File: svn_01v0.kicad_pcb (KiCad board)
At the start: 2 copper layers, 26 parts, among them J1 Screw_Terminal_01x05, Q1 IRF640, Q2 IRF640, U1 AD8542ARZ, U2 IR2110S, Y1 85kHz

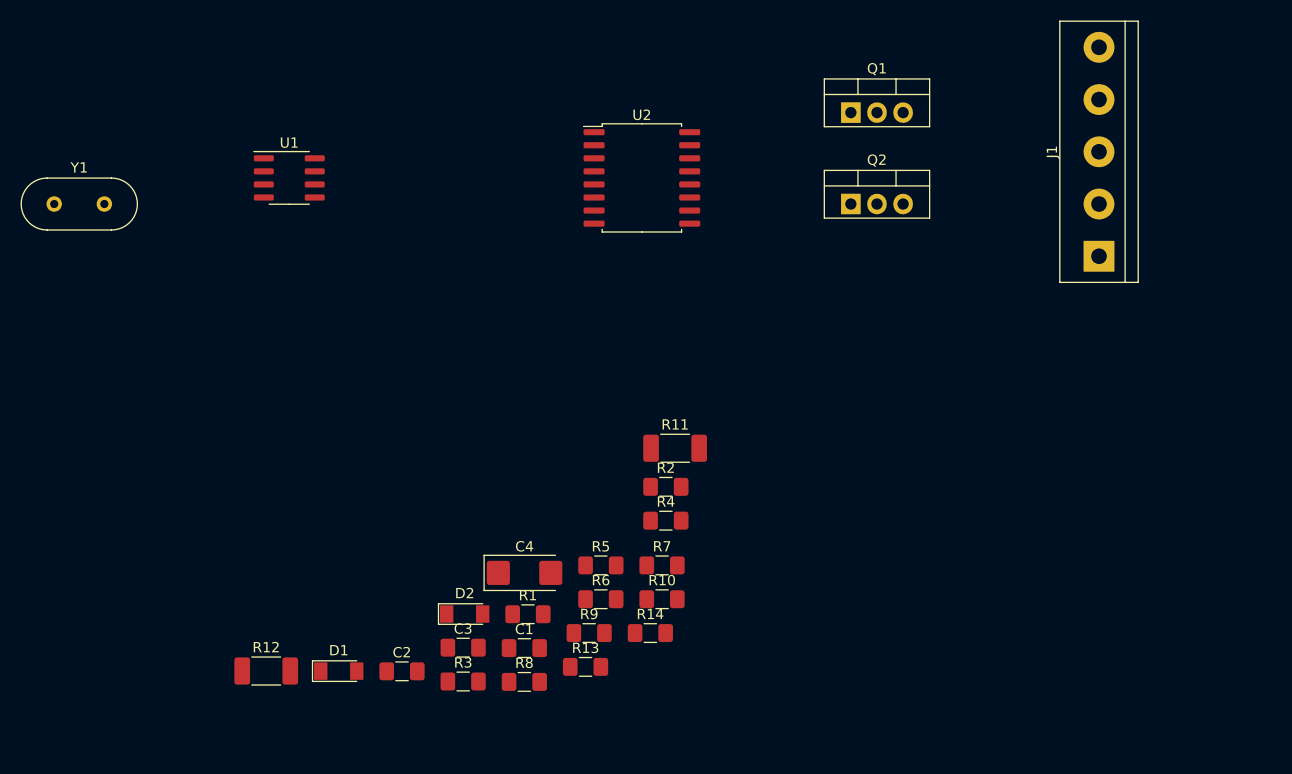
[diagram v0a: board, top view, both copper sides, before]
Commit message: Исправлена схема.
Исправлено подключенеи ОУ.
Разъем изменен на шести контактный.
Добавлен преобразователь 12В в 5В.
Добавлено несколько резисторов в обвязку ОУ.

Signed-off-by: bear.home <mihail_sheblykin@mail.ru>
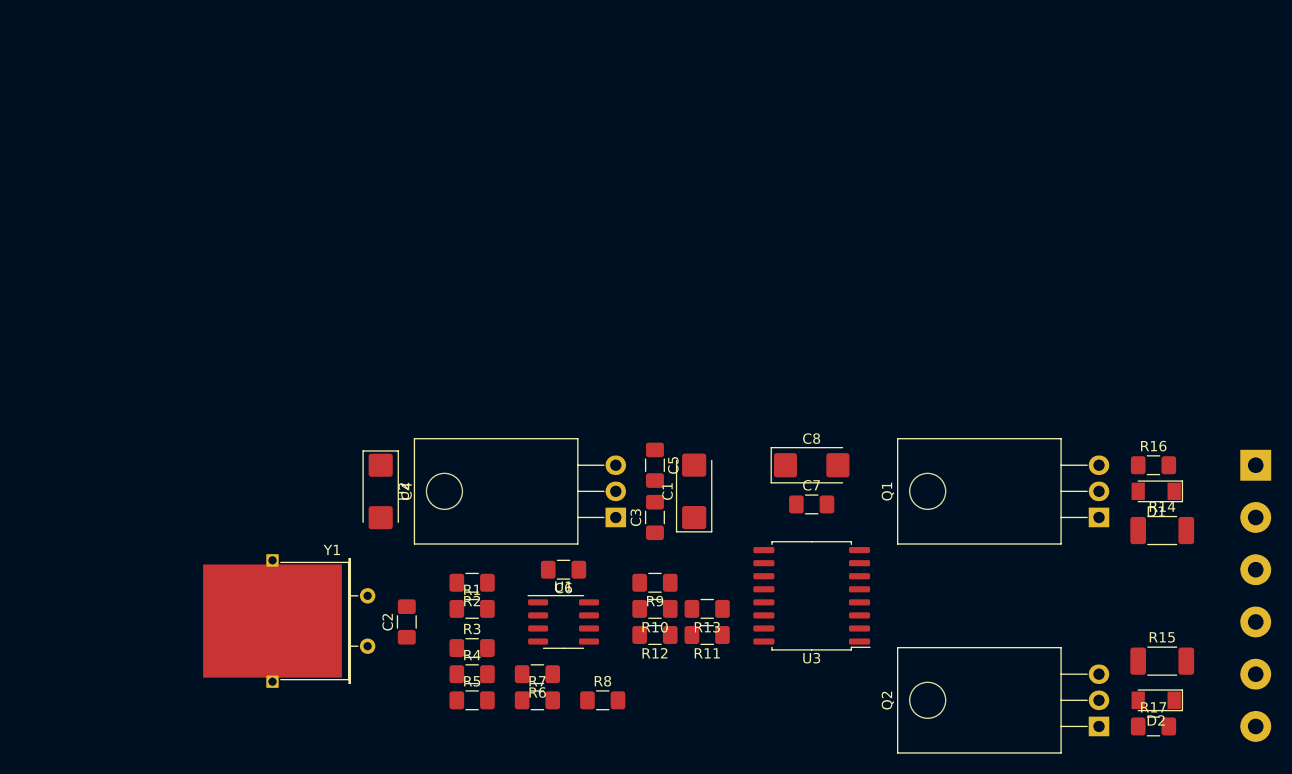
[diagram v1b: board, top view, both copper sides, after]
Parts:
- removed the R14 at (150.7, 90.0)
- added C1: 47uF x 16V, Capacitor_Tantalum_SMD:CP_EIA-6032-28_Kemet-C_Pad2.25x2.35mm_HandSolder, F.Cu at (154.9, 76.2)
- added C3: 100nF, Capacitor_SMD:C_1206_3216Metric_Pad1.42x1.75mm_HandSolder, F.Cu at (151.1, 78.7)
- added C4: 47uF x 16V, Capacitor_Tantalum_SMD:CP_EIA-6032-28_Kemet-C_Pad2.25x2.35mm_HandSolder, F.Cu at (124.5, 76.2)
- added C5: 100nF, Capacitor_SMD:C_1206_3216Metric_Pad1.42x1.75mm_HandSolder, F.Cu at (151.1, 73.7)
- added R12: 10k, Resistor_SMD:R_1206_3216Metric_Pad1.42x1.75mm_HandSolder, F.Cu at (151.1, 90.2)
- added R13: 10k, Resistor_SMD:R_1206_3216Metric_Pad1.42x1.75mm_HandSolder, F.Cu at (156.2, 87.6)
- added R17: 1k, Resistor_SMD:R_1206_3216Metric_Pad1.42x1.75mm_HandSolder, F.Cu at (199.6, 99.1)
- added R8: 10k, Resistor_SMD:R_1206_3216Metric_Pad1.42x1.75mm_HandSolder, F.Cu at (146.1, 96.5)
- added U2: LM7805_TO220, Package_TO_SOT_THT:TO-220-3_Horizontal_TabDown, F.Cu at (147.3, 78.7)
- C8: renamed from C4; value 22uF x 16V -> 47uF x 16V
- J1: value Screw_Terminal_01x05 -> Screw_Terminal_01x06; footprint TerminalBlock:TerminalBlock_bornier-5_P5.08mm -> TerminalBlock:TerminalBlock_bornier-6_P5.08mm; moved to B.Cu
- Q1, Q2: footprint Package_TO_SOT_THT:TO-220-3_Vertical -> Package_TO_SOT_THT:TO-220-3_Horizontal_TabDown
- R6: value 1k -> ?
- Y1: footprint Crystal:Crystal_HC49-U_Vertical -> Crystal:Crystal_HC49-U_Horizontal_1EP_style2
- moved R15 87.1 mm to (200.5, 92.7)
- moved D1 81.4 mm to (199.9, 76.2), turned to 180 degrees
- moved D2 67.8 mm to (199.9, 96.5), turned to 180 degrees
- moved R16 58.6 mm to (199.6, 73.7)
- moved Q2 56.2 mm to (194.3, 99.1), turned to 90 degrees
- moved U1 50.8 mm to (142.2, 88.9)
- moved Y1 48.8 mm to (123.2, 86.4), turned to 270 degrees
- moved R14 48.0 mm to (200.5, 80.0)
- moved Q1 46.2 mm to (194.3, 78.7), turned to 90 degrees
- moved U3 43.9 mm to (166.4, 86.4), turned to 180 degrees
- moved C7 36.6 mm to (166.4, 77.5)
- moved C8 29.8 mm to (166.4, 73.7)
- moved J1 25.4 mm to (209.6, 73.7), turned to 270 degrees
- moved R4 24.0 mm to (133.3, 94.0)
- moved R2 21.0 mm to (133.3, 85.1), turned to 180 degrees
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- renumbered C1 to C2, C2 to C6, C3 to C7, R8 to R11, R11 to R14, R12 to R15, R13 to R16, U2 to U3
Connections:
- C2 pad 1: Net-(C1-Pad1) -> Net-(C2-Pad1)
- J1 pad 2: +5V -> +12V
- R1 pad 2: Net-(C1-Pad1) -> Net-(C2-Pad1)
- R10 pad 1: +5V -> Net-(R10-Pad1)
- R11 pad 1: Net-(R8-Pad1) -> Net-(R11-Pad1)
- R11 pad 2: Net-(R10-Pad2) -> Net-(R10-Pad1)
- R7 pad 1: Net-(R10-Pad2) -> +5V
- R7 pad 2: Net-(R7-Pad2) -> Net-(R6-Pad1)
- R9 pad 1: Net-(R10-Pad2) -> Net-(R11-Pad1)
- R9 pad 2: GND -> Net-(R6-Pad1)
- U1 pad 2: Net-(R3-Pad2) -> Net-(C2-Pad1)
- U1 pad 3: Net-(C1-Pad1) -> Net-(R3-Pad2)
- U1 pad 5: Net-(R6-Pad1) -> Net-(R10-Pad2)
- U1 pad 6: Net-(R7-Pad2) -> Net-(R6-Pad1)
- U1 pad 7: Net-(R8-Pad1) -> Net-(R11-Pad1)
- U3 pad 14: Net-(R8-Pad1) -> Net-(R11-Pad1)
- Y1 pad 1: Net-(C1-Pad1) -> GND
- Y1 pad 2: GND -> Net-(C2-Pad1)
